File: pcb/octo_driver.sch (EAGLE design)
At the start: 19 parts, among them U1 LP2985-10DBVT

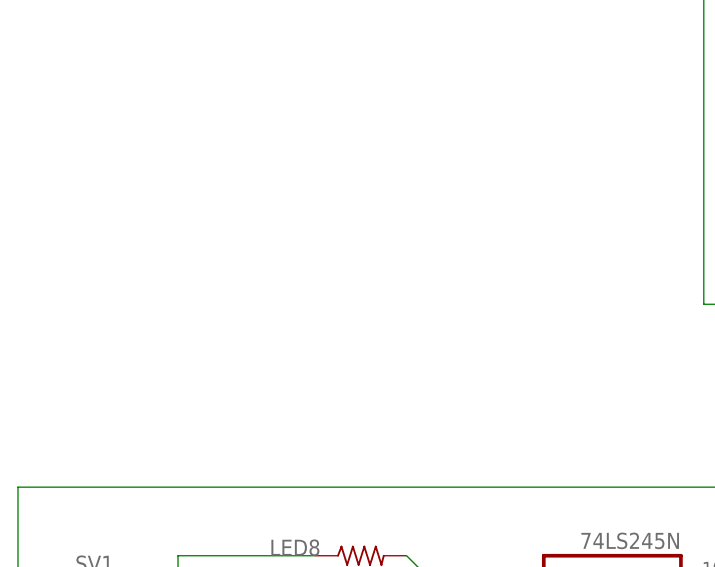
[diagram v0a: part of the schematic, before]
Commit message: added test pin for connecting a scope or multimeter
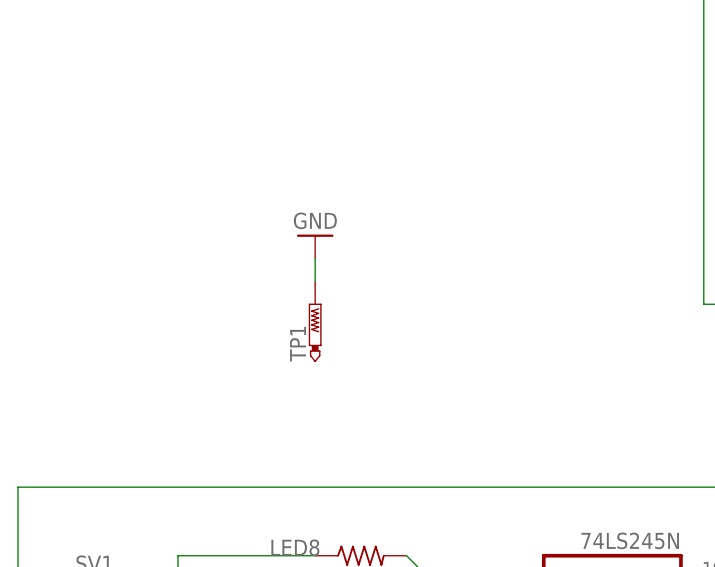
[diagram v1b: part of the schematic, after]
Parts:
- added TP1: PTR1B2,54, testpad:PTR1B2,54
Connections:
- net GND: now also TP1.TP
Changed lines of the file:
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@@
 <part name="C2" library="rcl" deviceset="C-US" device="C0805" value="1uF"/>
 <part name="GND4" library="supply1" deviceset="GND" device=""/>
+<part name="TP1" library="testpad" deviceset="PTR1" device="B2,54"/>
+<part name="GND5" library="supply1" deviceset="GND" device=""/>
 </parts>
 <sheets>
@@
 <instance part="C2" gate="G$1" x="58.42" y="101.6"/>
 <instance part="GND4" gate="1" x="106.68" y="71.12"/>
+<instance part="TP1" gate="G$1" x="0" y="76.2"/>
+<instance part="GND5" gate="1" x="0" y="83.82" rot="R180"/>
 </instances>
 <busses>
@@
 <wire x1="106.68" y1="78.74" x2="106.68" y2="73.66" width="0.1524" layer="91"/>
 </segment>
+<segment>
+<pinref part="TP1" gate="G$1" pin="TP"/>
+<pinref part="GND5" gate="1" pin="GND"/>
+<wire x1="0" y1="78.74" x2="0" y2="81.28" width="0.1524" layer="91"/>
+</segment>
 </net>

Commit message: fixed lots of warnings, general cleanup
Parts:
- removed TP1: PTR1B2,54, testpad:PTR1B2,54
- C3: value (none) -> 1uF
- JP1, SV1: value (none) -> (none)
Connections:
- new net N$2: C1.1, U1.VOUT
- net GND: now also H2.MOUNT, H3.MOUNT; no longer TP1.TP
- net VCC: no longer C1.1, U1.VOUT
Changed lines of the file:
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@@
 <part name="GND1" library="supply1" deviceset="GND" device=""/>
 <part name="GND2" library="supply1" deviceset="GND" device=""/>
-<part name="JP1" library="SparkFun-Connectors" deviceset="M02" device="PTH"/>
+<part name="JP1" library="SparkFun-Connectors" deviceset="M02" device="PTH" value=" "/>
 <part name="GND3" library="supply1" deviceset="GND" device=""/>
 <part name="RLED1" library="rcl" deviceset="R-US_" device="0207/2V" value="220"/>
@@
 <part name="H2" library="holes" deviceset="MOUNT-PAD-ROUND" device="2.8"/>
 <part name="H3" library="holes" deviceset="MOUNT-PAD-ROUND" device="2.8"/>
-<part name="C3" library="rcl" deviceset="C-US" device="C0805"/>
-<part name="SV1" library="penrose-con-lstb" deviceset="MA09-1" device=""/>
+<part name="C3" library="rcl" deviceset="C-US" device="C0805" value="1uF"/>
+<part name="SV1" library="penrose-con-lstb" deviceset="MA09-1" device="" value=" "/>
 <part name="U1" library="Texas Instruments_By_element14_Batch_1" deviceset="LP2985-10DBVT" device=""/>
 <part name="C1" library="rcl" deviceset="C-US" device="C0805" value="2.2uF"/>
 <part name="C2" library="rcl" deviceset="C-US" device="C0805" value="1uF"/>
 <part name="GND4" library="supply1" deviceset="GND" device=""/>
-<part name="TP1" library="testpad" deviceset="PTR1" device="B2,54"/>
-<part name="GND5" library="supply1" deviceset="GND" device=""/>
+<part name="P+2" library="supply1" deviceset="VCC" device=""/>
+<part name="P+3" library="supply1" deviceset="VCC" device=""/>
+<part name="P+4" library="supply1" deviceset="VCC" device=""/>
 </parts>
 <sheets>
@@
 <instance part="74HCT245" gate="P" x="17.78" y="2.54" rot="R90"/>
 <instance part="GND1" gate="1" x="35.56" y="2.54" rot="R90"/>
-<instance part="GND2" gate="1" x="50.8" y="45.72" rot="R90"/>
+<instance part="GND2" gate="1" x="45.72" y="50.8" rot="R180"/>
 <instance part="JP1" gate="G$1" x="33.02" y="154.94"/>
 <instance part="GND3" gate="1" x="53.34" y="152.4"/>
@@
 <instance part="C2" gate="G$1" x="58.42" y="101.6"/>
 <instance part="GND4" gate="1" x="106.68" y="71.12"/>
-<instance part="TP1" gate="G$1" x="0" y="76.2"/>
-<instance part="GND5" gate="1" x="0" y="83.82" rot="R180"/>
+<instance part="P+2" gate="VCC" x="116.84" y="45.72" rot="R270"/>
+<instance part="P+3" gate="VCC" x="5.08" y="5.08"/>
+<instance part="P+4" gate="VCC" x="50.8" y="43.18" rot="R270"/>
 </instances>
 <busses>
@@
 <pinref part="74HCT245" gate="A" pin="G"/>
 <pinref part="GND2" gate="1" pin="GND"/>
-<wire x1="48.26" y1="45.72" x2="45.72" y2="45.72" width="0.1524" layer="91"/>
+<wire x1="45.72" y1="48.26" x2="45.72" y2="45.72" width="0.1524" layer="91"/>
 </segment>
 <segment>
@@
 <wire x1="53.34" y1="154.94" x2="43.18" y2="154.94" width="0.1524" layer="91"/>
 <wire x1="43.18" y1="154.94" x2="40.64" y2="154.94" width="0.1524" layer="91"/>
-<wire x1="101.6" y1="162.56" x2="101.6" y2="152.4" width="0.1524" layer="91"/>
-<wire x1="101.6" y1="152.4" x2="101.6" y2="144.78" width="0.1524" layer="91"/>
-<wire x1="101.6" y1="152.4" x2="99.06" y2="152.4" width="0.1524" layer="91"/>
-<wire x1="99.06" y1="152.4" x2="73.66" y2="152.4" width="0.1524" layer="91"/>
-<wire x1="73.66" y1="152.4" x2="73.66" y2="154.94" width="0.1524" layer="91"/>
-<junction x="101.6" y="152.4"/>
 <wire x1="73.66" y1="154.94" x2="53.34" y2="154.94" width="0.1524" layer="91"/>
 <junction x="53.34" y="154.94"/>
-<pinref part="H1" gate="G$1" pin="MOUNT"/>
-<junction x="99.06" y="152.4"/>
 <wire x1="43.18" y1="154.94" x2="43.18" y2="111.76" width="0.1524" layer="91"/>
 <junction x="43.18" y="154.94"/>
@@
 <wire x1="58.42" y1="111.76" x2="43.18" y2="111.76" width="0.1524" layer="91"/>
 <junction x="43.18" y="111.76"/>
+<wire x1="73.66" y1="154.94" x2="73.66" y2="144.78" width="0.1524" layer="91"/>
+<pinref part="H3" gate="G$1" pin="MOUNT"/>
+<wire x1="73.66" y1="144.78" x2="96.52" y2="144.78" width="0.1524" layer="91"/>
+<wire x1="96.52" y1="144.78" x2="99.06" y2="144.78" width="0.1524" layer="91"/>
+<wire x1="96.52" y1="144.78" x2="96.52" y2="152.4" width="0.1524" layer="91"/>
+<pinref part="H1" gate="G$1" pin="MOUNT"/>
+<wire x1="96.52" y1="152.4" x2="99.06" y2="152.4" width="0.1524" layer="91"/>
+<wire x1="96.52" y1="152.4" x2="96.52" y2="162.56" width="0.1524" layer="91"/>
+<pinref part="H2" gate="G$1" pin="MOUNT"/>
+<wire x1="96.52" y1="162.56" x2="99.06" y2="162.56" width="0.1524" layer="91"/>
+<junction x="96.52" y="152.4"/>
+<junction x="96.52" y="162.56"/>
+<junction x="96.52" y="144.78"/>
 </segment>
 <segment>
@@
 <pinref part="GND4" gate="1" pin="GND"/>
 <wire x1="106.68" y1="78.74" x2="106.68" y2="73.66" width="0.1524" layer="91"/>
-</segment>
-<segment>
-<pinref part="TP1" gate="G$1" pin="TP"/>
-<pinref part="GND5" gate="1" pin="GND"/>
-<wire x1="0" y1="78.74" x2="0" y2="81.28" width="0.1524" layer="91"/>
 </segment>
 </net>
@@
 <segment>
 <pinref part="74HCT245" gate="A" pin="DIR"/>
-<wire x1="45.72" y1="43.18" x2="63.5" y2="43.18" width="0.1524" layer="91"/>
-<wire x1="63.5" y1="43.18" x2="63.5" y2="48.26" width="0.1524" layer="91"/>
+<pinref part="P+4" gate="VCC" pin="VCC"/>
+<wire x1="48.26" y1="43.18" x2="45.72" y2="43.18" width="0.1524" layer="91"/>
 </segment>
 <segment>
 <pinref part="TEENSY3.0" gate="G$1" pin="VIN"/>
-<wire x1="106.68" y1="45.72" x2="119.38" y2="45.72" width="0.1524" layer="91"/>
+<wire x1="106.68" y1="45.72" x2="114.3" y2="45.72" width="0.1524" layer="91"/>
+<pinref part="P+2" gate="VCC" pin="VCC"/>
 </segment>
 <segment>
@@
 <wire x1="5.08" y1="2.54" x2="5.08" y2="-7.62" width="0.1524" layer="91"/>
 <wire x1="5.08" y1="-7.62" x2="15.24" y2="-7.62" width="0.1524" layer="91"/>
-</segment>
+<pinref part="P+3" gate="VCC" pin="VCC"/>
+<junction x="5.08" y="2.54"/>
+</segment>
+</net>
+<net name="N$2" class="0">
 <segment>
 <pinref part="U1" gate="A" pin="VOUT"/>

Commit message: switched resistors to 0805 smt
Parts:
- RLED1, RLED10, RLED11, RLED12, RLED13, RLED14, RLED8, RLED9: device rcl:R-US_0207/2V -> rcl:R-US_R0805
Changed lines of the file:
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@@
 <part name="JP1" library="SparkFun-Connectors" deviceset="M02" device="PTH" value=" "/>
 <part name="GND3" library="supply1" deviceset="GND" device=""/>
-<part name="RLED1" library="rcl" deviceset="R-US_" device="0207/2V" value="220"/>
-<part name="RLED8" library="rcl" deviceset="R-US_" device="0207/2V" value="220"/>
-<part name="RLED9" library="rcl" deviceset="R-US_" device="0207/2V" value="220"/>
-<part name="RLED10" library="rcl" deviceset="R-US_" device="0207/2V" value="220"/>
-<part name="RLED11" library="rcl" deviceset="R-US_" device="0207/2V" value="220"/>
-<part name="RLED12" library="rcl" deviceset="R-US_" device="0207/2V" value="220"/>
-<part name="RLED13" library="rcl" deviceset="R-US_" device="0207/2V" value="220"/>
-<part name="RLED14" library="rcl" deviceset="R-US_" device="0207/2V" value="220"/>
+<part name="RLED1" library="rcl" deviceset="R-US_" device="R0805" value="220"/>
+<part name="RLED8" library="rcl" deviceset="R-US_" device="R0805" value="220"/>
+<part name="RLED9" library="rcl" deviceset="R-US_" device="R0805" value="220"/>
+<part name="RLED10" library="rcl" deviceset="R-US_" device="R0805" value="220"/>
+<part name="RLED11" library="rcl" deviceset="R-US_" device="R0805" value="220"/>
+<part name="RLED12" library="rcl" deviceset="R-US_" device="R0805" value="220"/>
+<part name="RLED13" library="rcl" deviceset="R-US_" device="R0805" value="220"/>
+<part name="RLED14" library="rcl" deviceset="R-US_" device="R0805" value="220"/>
 <part name="H1" library="holes" deviceset="MOUNT-PAD-ROUND" device="2.8"/>
 <part name="H2" library="holes" deviceset="MOUNT-PAD-ROUND" device="2.8"/>
